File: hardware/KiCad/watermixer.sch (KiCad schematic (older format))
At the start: 6 parts, among them U1 MCP4728

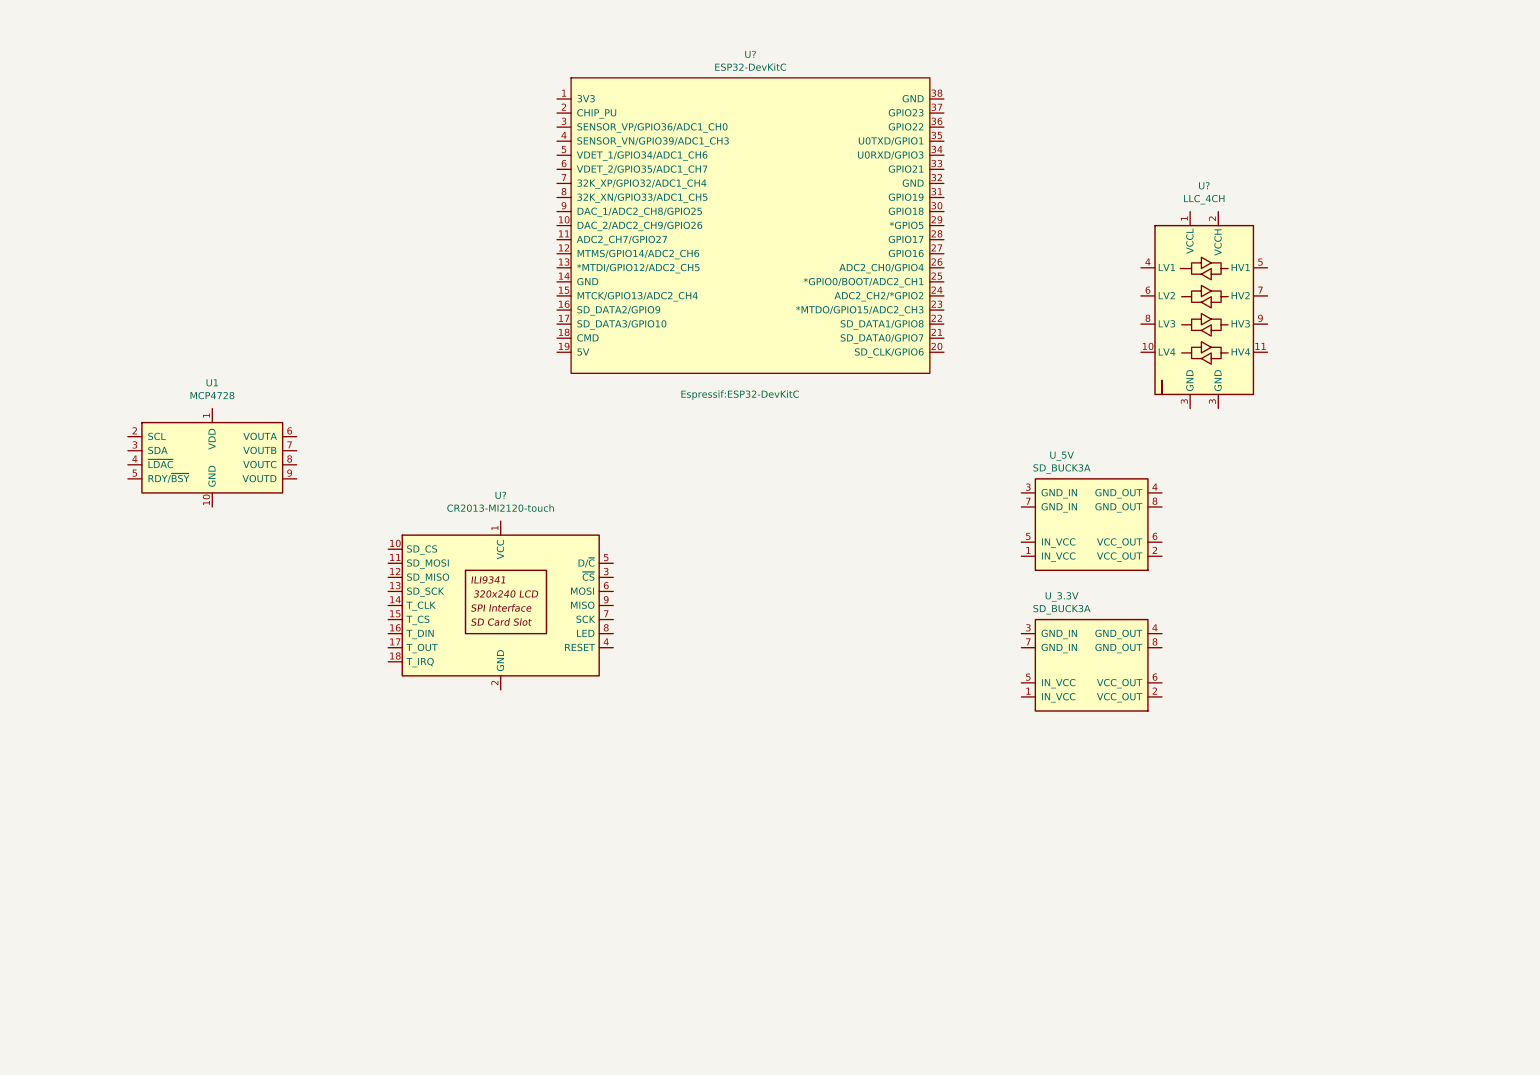
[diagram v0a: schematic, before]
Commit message: All Compoents created and added to Schematic
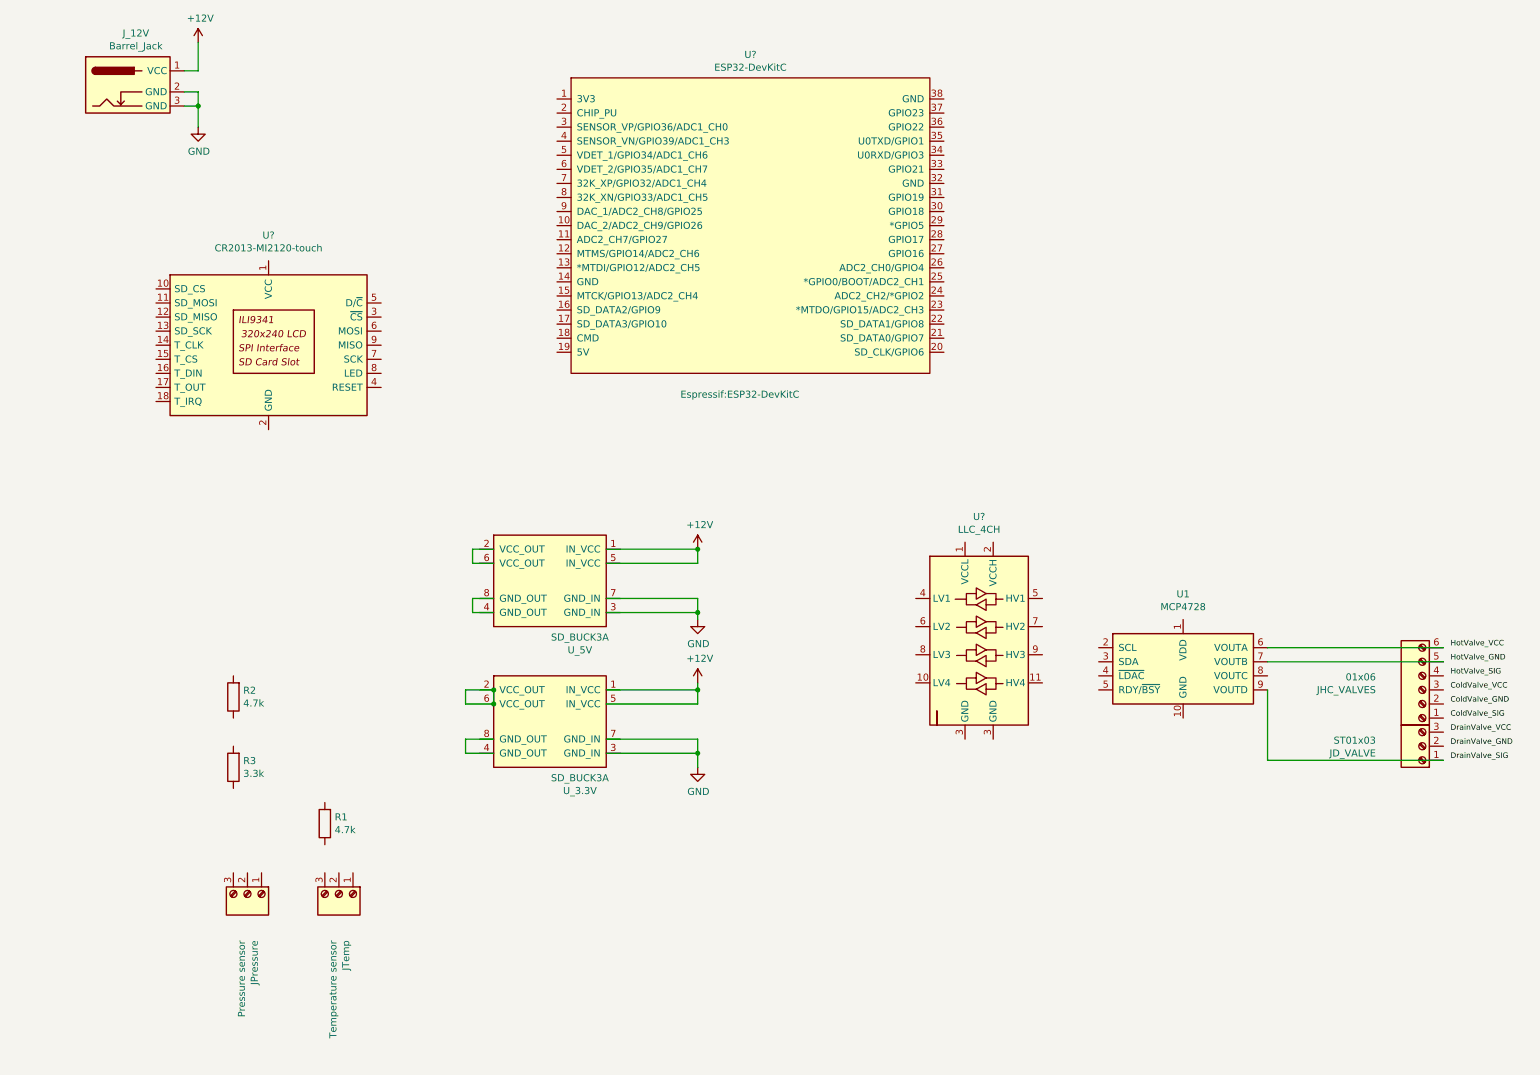
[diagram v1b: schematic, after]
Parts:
- added JD_VALVE: ST01x03, watermixer-footprints:Screw_Termianl_01x03, symbol watermixer-symbols:Screw_Terminal_01x03
- added JHC_VALVES: 01x06, watermixer-footprints:Screw_Termianl_01x06, symbol watermixer-symbols:Screw_Terminal_01x06
- added JPressure: Pressure sensor, watermixer-footprints:Screw_Termianl_01x03, symbol watermixer-symbols:Screw_Terminal_01x03
- added JTemp: Temperature sensor, watermixer-footprints:Screw_Termianl_01x03, symbol watermixer-symbols:Screw_Terminal_01x03
- added J_12V: Barrel_Jack, watermixer-footprints:Barrel_Jack, symbol watermixer-symbols:Barrel_Jack
- added R1, R2: 4.7k, Resistor_THT:R_Axial_DIN0207_L6.3mm_D2.5mm_P7.62mm_Horizontal, symbol watermixer-symbols:R
- added R3: 3.3k, Resistor_THT:R_Axial_DIN0207_L6.3mm_D2.5mm_P7.62mm_Horizontal, symbol watermixer-symbols:R
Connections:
- net labels added: +12V, ColdValve_GND, ColdValve_SIG, ColdValve_VCC, DrainValve_GND, DrainValve_SIG, DrainValve_VCC, GND, HotValve_GND, HotValve_SIG, HotValve_VCC
- wire segments 0 -> 38
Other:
- moved on the sheet: U1, U?, U_3.3V, U_5V

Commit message: Done connecting all parts on the schema
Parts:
- removed U?: CR2013-MI2120-touch, Display:CR2013-MI2120, symbol watermixer-symbols:CR2013-MI2120-touch
- added C1: 470uF, Capacitor_THT:CP_Radial_Tantal_D8.0mm_P5.00mm, symbol watermixer-symbols:CP
- added U?: Display, watermixer-footprints:CR2013-MI2120_touch, symbol watermixer-symbols:CR2013-MI2120-touch
- JD_VALVE: value ST01x03 -> 01x03
- renumbered JPressure to JPress
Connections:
- net labels added: 3.3V, 5V, SIG, VCC
- wire segments 38 -> 146
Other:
- moved on the sheet: JD_VALVE, JHC_VALVES, JPress, JTemp, J_12V, R1, R2, R3, U?, U_3.3V, U_5V

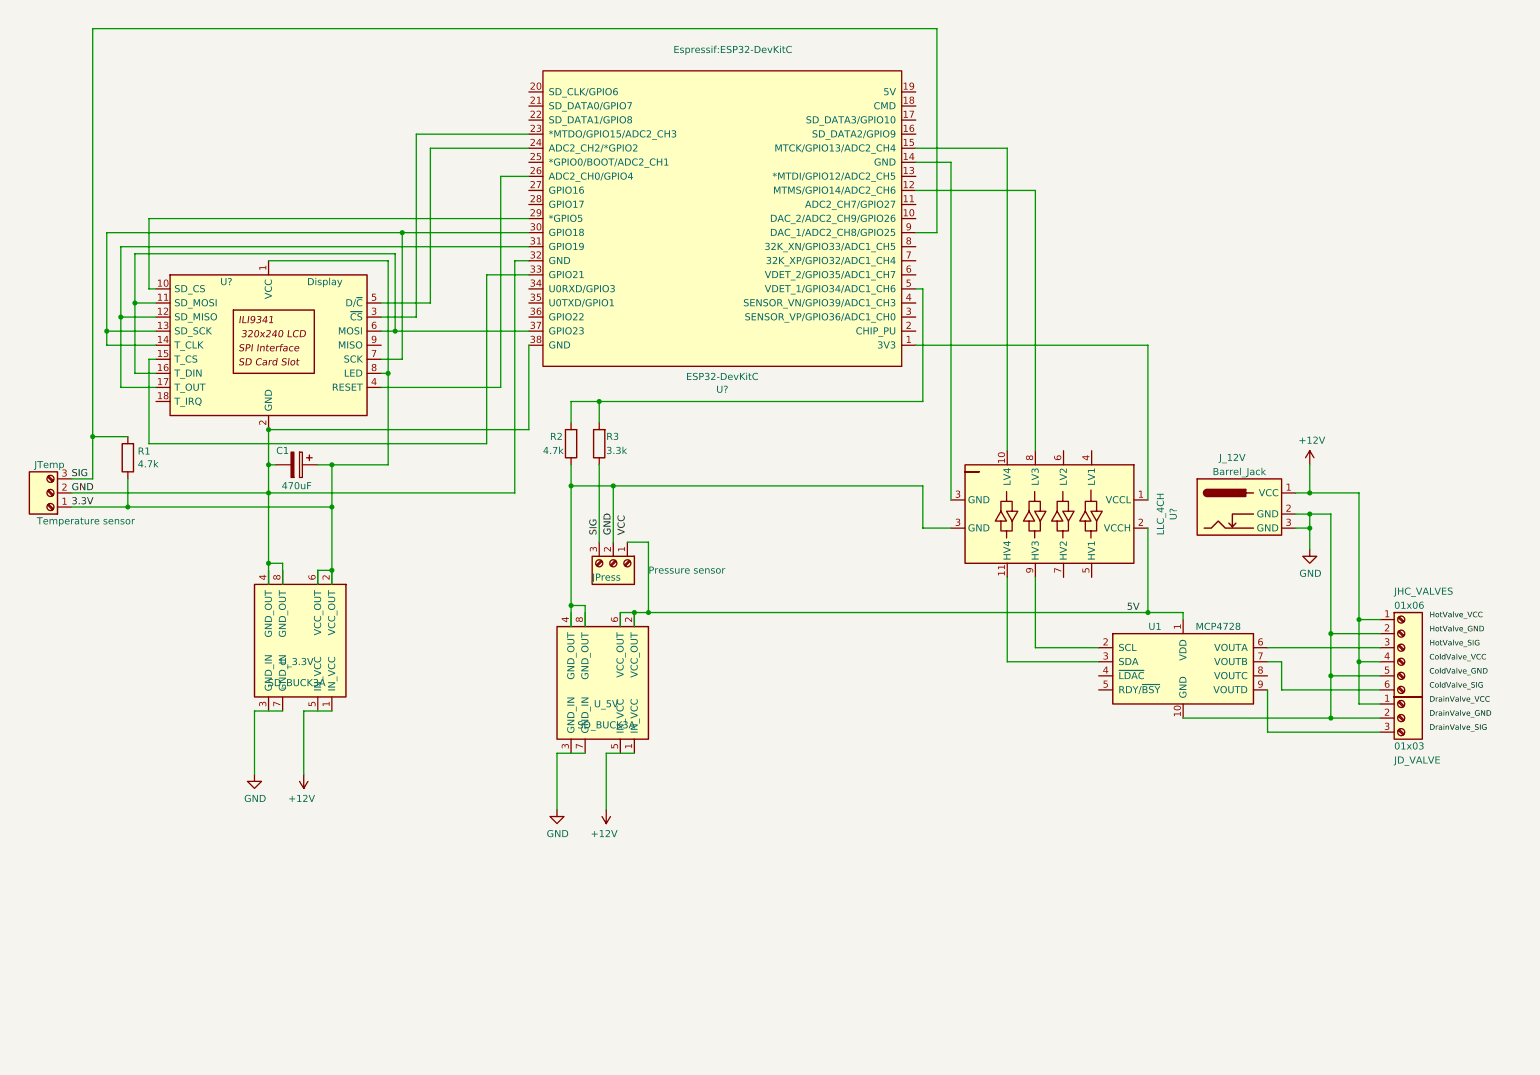
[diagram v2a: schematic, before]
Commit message: got a error free schematic
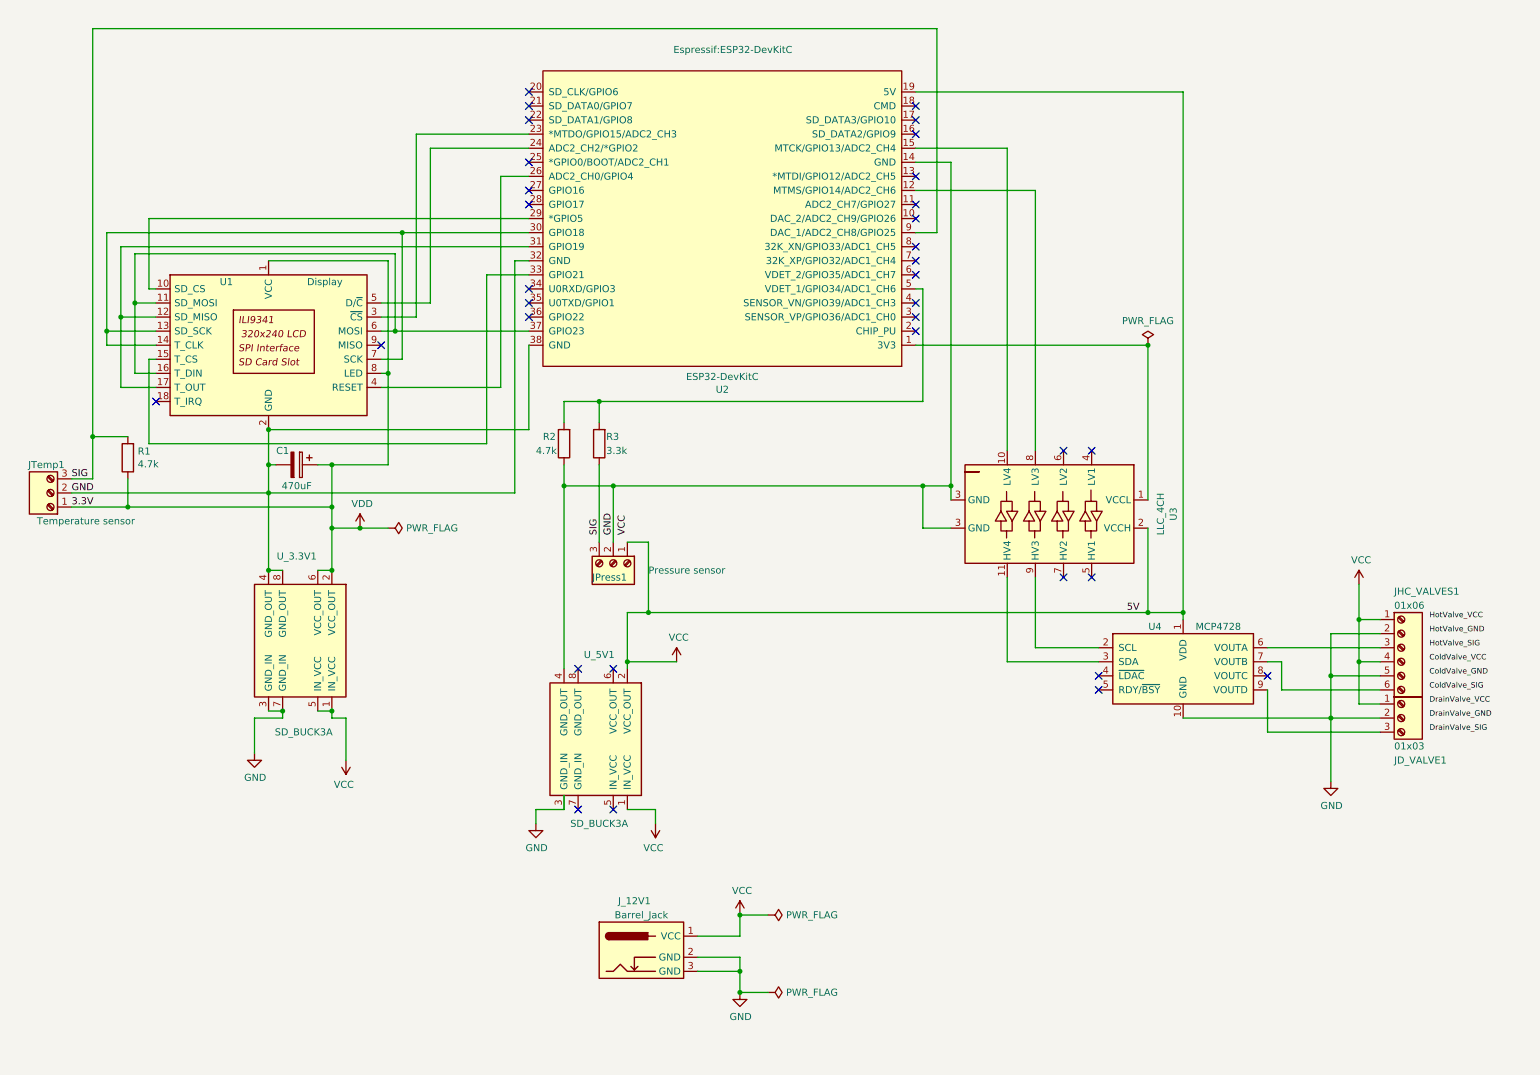
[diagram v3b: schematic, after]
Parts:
- gave numbers to parts that had none: 3
- renumbered JD_VALVE to JD_VALVE1, JHC_VALVES to JHC_VALVES1, JPress to JPress1, JTemp to JTemp1, J_12V to J_12V1, U1 to U4, U_3.3V to U_3.3V1, U_5V to U_5V1
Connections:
- net labels added: VDD
- net labels removed: +12V
- wire segments 146 -> 151
- no-connect marks 0 -> 34
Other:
- moved on the sheet: J_12V1, R2, U_5V1

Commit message: power fixes before running starting PCB editor
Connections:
- net GND: now also U_5V1.7 (GND_IN), U_5V1.8 (GND_OUT)
- net VCC: now also U_5V1.5 (IN_VCC); no longer JPress1.1, U2.19 (5V), U3.2 (VCCH), U4.1 (VDD), U_5V1.2 (VCC_OUT)
- net VDDF: now reaches U_5V1.6 (VCC_OUT)
- net VDDF: now also JPress1.1, U2.19 (5V), U3.2 (VCCH), U4.1 (VDD), U_5V1.2 (VCC_OUT)
- no-connect marks 34 -> 30
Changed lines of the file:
@@
 NoConn ~ 1400 3350
 $Comp
-L power:VCC #PWR06
+L power:VCC #PWR07
 U 1 1 615867D1
 P 5550 7000
-F 0 "#PWR06" H 5550 6850 50  0001 C CNN
+F 0 "#PWR07" H 5550 6850 50  0001 C CNN
 F 1 "VCC" H 5565 7173 50  0000 C CNN
 F 2 "" H 5550 7000 50  0001 C CNN
@@
 	5550 7150 5550 7000
 $Comp
-L power:GND #PWR07
+L power:GND #PWR08
 U 1 1 6158DE4A
 P 5550 7550
-F 0 "#PWR07" H 5550 7300 50  0001 C CNN
+F 0 "#PWR08" H 5550 7300 50  0001 C CNN
 F 1 "GND" H 5555 7377 50  0000 C CNN
 F 2 "" H 5550 7550 50  0001 C CNN
@@
 $EndComp
 $Comp
-L power:VCC #PWR09
+L power:VCC #PWR010
 U 1 1 615AFAED
 P 9950 4650
-F 0 "#PWR09" H 9950 4500 50  0001 C CNN
+F 0 "#PWR010" H 9950 4500 50  0001 C CNN
 F 1 "VCC" H 9965 4823 50  0000 C CNN
 F 2 "" H 9950 4650 50  0001 C CNN
@@
 $EndComp
 $Comp
-L power:GND #PWR08
+L power:GND #PWR09
 U 1 1 615B0DF3
 P 9750 6050
-F 0 "#PWR08" H 9750 5800 50  0001 C CNN
+F 0 "#PWR09" H 9750 5800 50  0001 C CNN
 F 1 "GND" H 9755 5877 50  0000 C CNN
 F 2 "" H 9750 6050 50  0001 C CNN
@@
 $EndComp
 $Comp
-L power:VCC #PWR04
+L power:VCC #PWR05
 U 1 1 615F4805
 P 4950 6350
-F 0 "#PWR04" H 4950 6200 50  0001 C CNN
+F 0 "#PWR05" H 4950 6200 50  0001 C CNN
 F 1 "VCC" H 4965 6523 50  0000 C CNN
 F 2 "" H 4950 6350 50  0001 C CNN
@@
 $EndComp
 $Comp
-L power:GND #PWR03
+L power:GND #PWR04
 U 1 1 615F4C68
 P 4100 6350
-F 0 "#PWR03" H 4100 6100 50  0001 C CNN
+F 0 "#PWR04" H 4100 6100 50  0001 C CNN
 F 1 "GND" H 4105 6177 50  0000 C CNN
 F 2 "" H 4100 6350 50  0001 C CNN
@@
 Wire Wire Line
 	4100 6250 4300 6250
-NoConn ~ 4400 6250
-NoConn ~ 4650 6250
-NoConn ~ 4400 5250
-NoConn ~ 4650 5250
 Wire Wire Line
 	2650 5600 2650 5550
@@
 	2200 4550 2200 4000
 Connection ~ 2650 4100
-Wire Wire Line
-	4750 5250 4750 5200
 Wire Wire Line
 	4750 4850 4900 4850
@@
 	950  3900 950  3600
 Connection ~ 950  3600
-Connection ~ 4750 5200
-Wire Wire Line
-	4750 5200 4750 4850
 Wire Wire Line
 	6800 2950 8450 2950
@@
 $EndComp
 Connection ~ 8450 2950
-$Comp
-L power:VCC #PWR05
-U 1 1 61776287
-P 5100 5200
-F 0 "#PWR05" H 5100 5050 50  0001 C CNN
-F 1 "VCC" H 5115 5373 50  0000 C CNN
-F 2 "" H 5100 5200 50  0001 C CNN
-F 3 "" H 5100 5200 50  0001 C CNN
-	1    5100 5200
-	1    0    0    -1
-$EndComp
-Wire Wire Line
-	5100 5200 4750 5200
 Wire Wire Line
 	5750 7000 5550 7000
@@
 NoConn ~ 3000 2950
 $Comp
-L power:VDD #PWR0101
+L power:VDD #PWR03
 U 1 1 617A9ADE
 P 2850 4250
-F 0 "#PWR0101" H 2850 4100 50  0001 C CNN
+F 0 "#PWR03" H 2850 4100 50  0001 C CNN
 F 1 "VDD" H 2865 4423 50  0000 C CNN
 F 2 "" H 2850 4250 50  0001 C CNN
@@
 	2650 4250 2650 4550
 $Comp
-L power:PWR_FLAG #FLG0101
+L power:PWR_FLAG #FLG01
 U 1 1 617B04F0
 P 3050 4250
-F 0 "#FLG0101" H 3050 4325 50  0001 C CNN
+F 0 "#FLG01" H 3050 4325 50  0001 C CNN
 F 1 "PWR_FLAG" V 3050 4378 50  0000 L CNN
 F 2 "" H 3050 4250 50  0001 C CNN
@@
 	3050 4250 2850 4250
 Connection ~ 2850 4250
+Wire Wire Line
+	4400 5250 4300 5250
+Connection ~ 4300 5250
+Wire Wire Line
+	4650 5250 4750 5250
+Connection ~ 4750 5250
+Wire Wire Line
+	4650 6250 4750 6250
+Connection ~ 4750 6250
+Wire Wire Line
+	4400 6250 4300 6250
+Connection ~ 4300 6250
+$Comp
+L power:VDDF #PWR06
+U 1 1 61442B2C
+P 5100 5100
+F 0 "#PWR06" H 5100 4950 50  0001 C CNN
+F 1 "VDDF" H 5115 5273 50  0000 C CNN
+F 2 "" H 5100 5100 50  0001 C CNN
+F 3 "" H 5100 5100 50  0001 C CNN
+	1    5100 5100
+	1    0    0    -1
+$EndComp
+$Comp
+L power:PWR_FLAG #FLG02
+U 1 1 61443F0F
+P 5500 5100
+F 0 "#FLG02" H 5500 5175 50  0001 C CNN
+F 1 "PWR_FLAG" H 5500 5273 50  0000 C CNN
+F 2 "" H 5500 5100 50  0001 C CNN
+F 3 "~" H 5500 5100 50  0001 C CNN
+	1    5500 5100
+	1    0    0    -1
+$EndComp
+Wire Wire Line
+	4750 4850 4750 5100
+Wire Wire Line
+	5500 5100 5100 5100
+Wire Wire Line
+	5100 5100 4750 5100
+Connection ~ 5100 5100
+Connection ~ 4750 5100
+Wire Wire Line
+	4750 5100 4750 5250
 $EndSCHEMATC
